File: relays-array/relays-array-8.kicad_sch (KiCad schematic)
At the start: 61 parts, among them J1 NMJ6HCD2, J10 Screw_Terminal_01x02, J11 NMJ6HCD2, J12 NMJ6HCD2, J13 Screw_Terminal_01x02, J14 NMJ6HCD2, J15 Screw_Terminal_01x02, J2 NMJ6HCD2, J3 Screw_Terminal_01x02, J4 NMJ6HCD2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

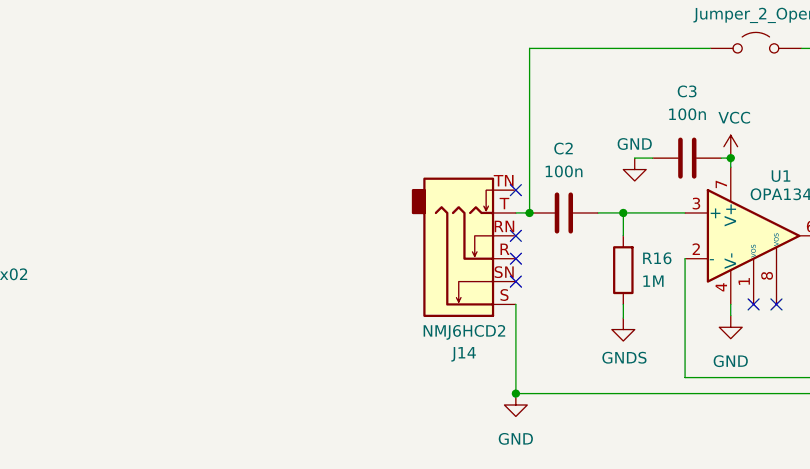
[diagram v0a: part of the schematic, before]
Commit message: relays-array: add terminal block for buffer use w/ external connector
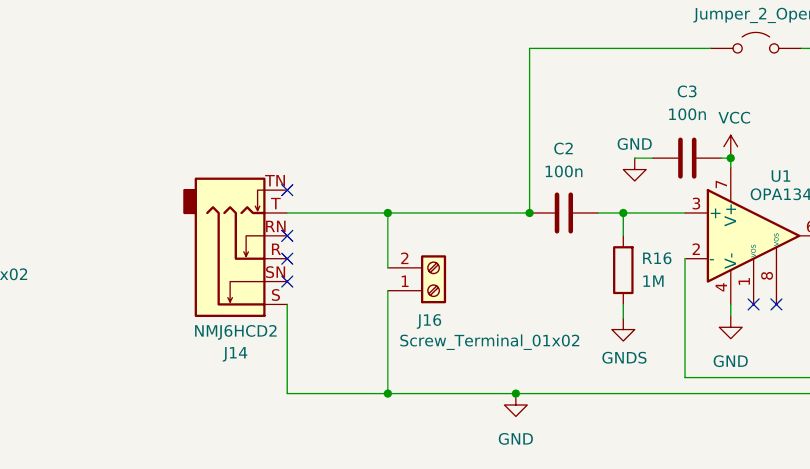
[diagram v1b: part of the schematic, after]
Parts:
- added J16: Screw_Terminal_01x02, TerminalBlock:TerminalBlock_bornier-2_P5.08mm, symbol Connector:Screw_Terminal_01x02
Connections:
- net GND: now also J16.1 (Pin_1)
- net at C2.2, J14.T, JPX1.2 (B): now also J16.2 (Pin_2)
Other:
- moved on the sheet: J14
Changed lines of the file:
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@@
 	)
 	(junction
+		(at 223.774 199.136)
+		(diameter 0)
+		(color 0 0 0 0)
+	)
+	(junction
 		(at 282.448 219.202)
 		(diameter 0)
@@
 	)
 	(junction
-		(at 237.998 219.202)
+		(at 352.044 55.88)
 		(diameter 0)
 		(color 0 0 0 0)
 	)
 	(junction
-		(at 352.044 55.88)
+		(at 223.774 219.202)
 		(diameter 0)
 		(color 0 0 0 0)
@@
 	)
 	(junction
+		(at 237.998 219.202)
+		(diameter 0)
+		(color 0 0 0 0)
+	)
+	(junction
 		(at 74.168 73.66)
 		(diameter 0)
@@
 	)
 	(no_connect
-		(at 237.998 196.596)
+		(at 212.598 196.596)
 	)
 	(no_connect
@@
 	)
 	(no_connect
-		(at 237.998 204.216)
+		(at 212.598 204.216)
 	)
 	(no_connect
@@
 	)
 	(no_connect
-		(at 237.998 201.676)
+		(at 212.598 201.676)
 	)
 	(no_connect
@@
 	)
 	(no_connect
-		(at 237.998 206.756)
+		(at 212.598 206.756)
 	)
 	(no_connect
@@
 	(wire
 		(pts
-			(xy 88.138 58.42) (xy 88.138 105.156)
+			(xy 223.774 207.772) (xy 223.774 219.202)
 		)
 		(stroke
@@
 	(wire
 		(pts
-			(xy 227.584 115.824) (xy 233.934 115.824)
+			(xy 88.138 58.42) (xy 88.138 105.156)
 		)
 		(stroke
@@
 	(wire
 		(pts
-			(xy 237.998 219.202) (xy 282.448 219.202)
+			(xy 227.584 115.824) (xy 233.934 115.824)
 		)
 		(stroke
@@
 	(wire
 		(pts
-			(xy 349.504 73.66) (xy 358.394 73.66)
+			(xy 237.998 219.202) (xy 282.448 219.202)
 		)
 		(stroke
@@
 	(wire
 		(pts
-			(xy 227.584 125.984) (xy 233.934 125.984)
+			(xy 349.504 73.66) (xy 358.394 73.66)
 		)
 		(stroke
@@
 	(wire
 		(pts
-			(xy 237.998 199.136) (xy 239.522 199.136)
+			(xy 227.584 125.984) (xy 233.934 125.984)
 		)
 		(stroke
@@
 	(wire
 		(pts
+			(xy 237.998 219.202) (xy 223.774 219.202)
+		)
+		(stroke
+			(width 0)
+			(type default)
+		)
+	)
+	(wire
+		(pts
 			(xy 231.394 92.964) (xy 231.394 105.664)
 		)
@@
 	(wire
 		(pts
+			(xy 212.598 199.136) (xy 223.774 199.136)
+		)
+		(stroke
+			(width 0)
+			(type default)
+		)
+	)
+	(wire
+		(pts
 			(xy 138.684 92.964) (xy 145.034 92.964)
 		)
@@
 	(wire
 		(pts
+			(xy 223.774 199.136) (xy 239.522 199.136)
+		)
+		(stroke
+			(width 0)
+			(type default)
+		)
+	)
+	(wire
+		(pts
 			(xy 47.498 43.18) (xy 53.848 43.18)
 		)
@@
 	(wire
 		(pts
+			(xy 212.598 219.202) (xy 212.598 209.296)
+		)
+		(stroke
+			(width 0)
+			(type default)
+		)
+	)
+	(wire
+		(pts
 			(xy 348.742 112.776) (xy 357.632 112.776)
 		)
@@
 	(wire
 		(pts
-			(xy 237.998 209.296) (xy 237.998 219.202)
-		)
-		(stroke
-			(width 0)
-			(type default)
-		)
-	)
-	(wire
-		(pts
 			(xy 349.504 63.5) (xy 358.394 63.5)
 		)
@@
 	(wire
 		(pts
+			(xy 223.774 219.202) (xy 212.598 219.202)
+		)
+		(stroke
+			(width 0)
+			(type default)
+		)
+	)
+	(wire
+		(pts
 			(xy 138.684 92.964) (xy 138.684 105.664)
 		)
@@
 	(wire
 		(pts
+			(xy 223.774 199.136) (xy 223.774 205.232)
+		)
+		(stroke
+			(width 0)
+			(type default)
+		)
+	)
+	(wire
+		(pts
 			(xy 247.142 199.136) (xy 249.936 199.136)
 		)
@@
 	(symbol
 		(lib_id "Connector_Audio:NMJ6HCD2")
-		(at 232.918 204.216 0)
+		(at 207.518 204.216 0)
 		(mirror x)
 		(unit 1)
@@
 		(dnp no)
 		(property "Reference" "J14"
-			(at 232.283 214.7105 0)
+			(at 206.883 214.7105 0)
 			(effects
 				(font
@@
 		)
 		(property "Value" "NMJ6HCD2"
-			(at 232.283 212.2862 0)
+			(at 206.883 212.2862 0)
 			(effects
 				(font
@@
 		)
 		(property "Footprint" "Connector_Audio:Jack_6.35mm_Neutrik_NMJ6HCD2_Horizontal"
-			(at 232.918 204.216 0)
+			(at 207.518 204.216 0)
 			(effects
 				(font
@@
 		)
 		(property "Datasheet" "https://www.neutrik.com/en/product/nmj6hcd2"
-			(at 232.918 204.216 0)
+			(at 207.518 204.216 0)
 			(effects
 				(font
@@
 		)
 		(property "Description" "M Series, 6.35mm (1/4in) stereo jack, switched, with chrome ferrule and straight PCB pins"
-			(at 232.918 204.216 0)
+			(at 207.518 204.216 0)
 			(effects
 				(font
@@
 					(unit 1)
 				)
+			)
+		)
+	)
+	(symbol
+		(lib_id "Connector:Screw_Terminal_01x02")
+		(at 228.854 207.772 0)
+		(mirror x)
+		(unit 1)
+		(exclude_from_sim no)
+		(in_bom yes)
+		(on_board yes)
+		(dnp no)
+		(property "Reference" "J16"
+			(at 227.076 211.074 0)
+			(effects
+				(font
+					(size 1.27 1.27)
+				)
+				(justify left)
+			)
+		)
+		(property "Value" "Screw_Terminal_01x02"
+			(at 225.044 213.36 0)
+			(effects
+				(font
+					(size 1.27 1.27)
+				)
+				(justify left)
+			)
+		)
+		(property "Footprint" "TerminalBlock:TerminalBlock_bornier-2_P5.08mm"
+			(at 228.854 207.772 0)
+			(effects
+				(font
+					(size 1.27 1.27)
+				)
+				(hide yes)
+			)
+		)
+		(property "Datasheet" "~"
+			(at 228.854 207.772 0)
+			(effects
+				(font
+					(size 1.27 1.27)
+				)
+				(hide yes)
+			)
+		)
+		(property "Description" "Generic screw terminal, single row, 01x02, script generated (kicad-library-utils/schlib/autogen/connector/)"
+			(at 228.854 207.772 0)
+			(effects
+				(font
+					(size 1.27 1.27)
+				)
+				(hide yes)
+			)
+		)
+		(pin "2"
+		)
+		(pin "1"
+		)
+		(instances
+			(project "relays-array-8"
+				(path "/0ea4a1ad-93c5-49ff-94da-e7ea5c0fdbe6"
+					(reference "J16")
+					(unit 1)
+				)

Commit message: relays-array: fix schematics error and add ground plane
The jack connectors are all (except for the buffer input) wired
backwards, with the tip going to `GND` and the sleeve on `SIGNAL`, while
it should be the other way around.

While at it, improve a bit the PCB tracks and add a ground plane. The
latter is only connected to `GND` in a single point in order to avoid
ground loops and other unpleasant issues.
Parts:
- added JP1: Jumper_2_Bridged, Jumper:SolderJumper-2_P1.3mm_Bridged_RoundedPad1.0x1.5mm, symbol Jumper:Jumper_2_Bridged
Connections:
- net GND: now also K1.14, K2.14, K3.14, K4.14, K5.14, K6.14, K7.14, K8.14, JP1.2 (B); no longer K1.24, K2.24, K3.24, K4.24, K5.24, K6.24, K7.24, K8.24
- net SIGNAL: now also K1.24, K2.24, K3.24, K4.24, K5.24, K6.24, K7.24, K8.24; no longer K1.14, K2.14, K3.14, K4.14, K5.14, K6.14, K7.14, K8.14
- new net Earth: JP1.1 (A)
